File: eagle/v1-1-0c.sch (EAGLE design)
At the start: 177 parts, among them J1 CR22A-44D-2.54DSA(70), J3 26-60-4040, J4 AUDIO_JACK_3.5MM_PTH, J5 DIN5, SW1 3PDT-AQ-SWITCH, SW2 9077-1, U10 7805, U11 74LS10N, U13 74LS04N, U14 4528N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

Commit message: Errata updates to BRD and SCH and PDFs
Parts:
- added JP5, JP6: (no value), aquarius2:PINHD-1X1
- R49: device aq-rcl:R-US_0207/7 -> aq-rcl:R-US_0207/10
- R50, R51: value ∞/56k -> ∞/1.5k
- R52: value ∞/56k -> ∞/100
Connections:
- new net 2Φ-NTSC: JP5.1, U11A.O
- net 2Φ: now also JP6.1; no longer U11A.O
- net GND: no longer R49.1
- net VCC: now also R49.1
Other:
- note added: "(NTSC to GND)"
- note added: "(PAL through R49)"
- note added: "18 OCT 2020"
- note added: "NTSC Close for 2Φ"
- note removed: "(NTSC passthrough)"
- note removed: "05 SEP 2020"
- moved on the sheet: R49
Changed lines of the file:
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@@
 <part name="C2" library="aq-rcl" deviceset="C-US" device="050-024X044" package3d_urn="urn:adsk.eagle:package:23643/1" value="10pF"/>
 <part name="C25" library="aq-rcl" deviceset="C-US" device="050-025X090" value=".1uF"/>
-<part name="R49" library="aq-rcl" deviceset="R-US_" device="0207/7" package3d_urn="urn:adsk.eagle:package:23493/2" value="0/220"/>
 <part name="C37" library="aq-rcl" deviceset="C-US" device="025-030X050" package3d_urn="urn:adsk.eagle:package:23631/1" value=".001uF/∞"/>
 <part name="C1" library="aq-rcl" deviceset="CPOL-US" device="E2.5-6" package3d_urn="urn:adsk.eagle:package:23349/1" value="1uF @ 50v"/>
@@
 <part name="GND37" library="supply1" library_urn="urn:adsk.eagle:library:371" deviceset="GND" device=""/>
 <part name="P+11" library="supply1" library_urn="urn:adsk.eagle:library:371" deviceset="VCC" device=""/>
-<part name="GND13" library="supply1" library_urn="urn:adsk.eagle:library:371" deviceset="GND" device=""/>
 <part name="SUPPLY13" library="supply2" library_urn="urn:adsk.eagle:library:372" deviceset="VPP" device=""/>
 <part name="C23" library="aq-rcl" deviceset="C-US" device="050-024X044" package3d_urn="urn:adsk.eagle:package:23643/1" value="∞/10pF"/>
-<part name="R50" library="aq-rcl" deviceset="R-US_" device="0207/10" package3d_urn="urn:adsk.eagle:package:23491/2" value="∞/56k"/>
-<part name="R51" library="aq-rcl" deviceset="R-US_" device="0207/10" package3d_urn="urn:adsk.eagle:package:23491/2" value="∞/56k"/>
+<part name="R50" library="aq-rcl" deviceset="R-US_" device="0207/10" package3d_urn="urn:adsk.eagle:package:23491/2" value="∞/1.5k"/>
+<part name="R51" library="aq-rcl" deviceset="R-US_" device="0207/10" package3d_urn="urn:adsk.eagle:package:23491/2" value="∞/1.5k"/>
 <part name="XTAL2" library="special" library_urn="urn:adsk.eagle:library:367" deviceset="XTAL" device="" package3d_urn="urn:adsk.eagle:package:26649/1" value="∞/7.15909 Mhz"/>
-<part name="R52" library="aq-rcl" deviceset="R-US_" device="0207/10" package3d_urn="urn:adsk.eagle:package:23491/2" value="∞/56k"/>
+<part name="R52" library="aq-rcl" deviceset="R-US_" device="0207/10" package3d_urn="urn:adsk.eagle:package:23491/2" value="∞/100"/>
 <part name="U13" library="74xx-us" library_urn="urn:adsk.eagle:library:88" deviceset="74*04" device="N" package3d_urn="urn:adsk.eagle:package:16407/2" technology="LS"/>
 <part name="C43" library="aq-rcl" deviceset="C-US" device="050-025X090" value="∞/0.1uF"/>
@@
 <part name="SUPPLY12" library="supply2" library_urn="urn:adsk.eagle:library:372" deviceset="VEE" device=""/>
 <part name="J2" library="aquarius2" deviceset="PINHD-1X17" device="" package3d_urn="urn:adsk.eagle:package:22490/2"/>
+<part name="R49" library="aq-rcl" deviceset="R-US_" device="0207/10" package3d_urn="urn:adsk.eagle:package:23491/2" value="0/220"/>
+<part name="P+21" library="supply1" library_urn="urn:adsk.eagle:library:371" deviceset="VCC" device=""/>
+<part name="GND13" library="supply1" library_urn="urn:adsk.eagle:library:371" deviceset="GND" device=""/>
+<part name="JP5" library="aquarius2" deviceset="PINHD-1X1" device="" package3d_urn="urn:adsk.eagle:package:22485/2"/>
+<part name="JP6" library="aquarius2" deviceset="PINHD-1X1" device="" package3d_urn="urn:adsk.eagle:package:22485/2"/>
 </parts>
 <sheets>
@@
 <wire x1="261.62" y1="15.24" x2="261.62" y2="5.08" width="0.1524" layer="97"/>
 <wire x1="261.62" y1="5.08" x2="347.98" y2="5.08" width="0.1524" layer="97"/>
-<text x="304.8" y="7.62" size="5.08" layer="97" align="bottom-center">05 SEP 2020</text>
+<text x="304.8" y="7.62" size="5.08" layer="97" align="bottom-center">18 OCT 2020</text>
 <wire x1="347.98" y1="15.24" x2="347.98" y2="25.4" width="0.1524" layer="97"/>
 <wire x1="347.98" y1="25.4" x2="261.62" y2="25.4" width="0.1524" layer="97"/>
@@
 <wire x1="76.708" y1="59.436" x2="60.198" y2="59.436" width="0.1524" layer="97" style="shortdash"/>
 <wire x1="59.436" y1="59.436" x2="59.436" y2="67.818" width="0.1524" layer="97" style="shortdash"/>
-<text x="338.836" y="188.214" size="1.778" layer="97" distance="25" align="center">(NTSC passthrough)</text>
-<text x="343.916" y="194.056" size="1.016" layer="97" distance="25" rot="R180" align="center">NTSC to JP4
+<text x="343.154" y="187.96" size="1.27" layer="97" distance="25" align="center">(NTSC to GND)</text>
+<text x="344.424" y="195.072" size="1.016" layer="97" distance="25" rot="R180" align="center">NTSC to JP4
 TEA1002 PALSW</text>
 <text x="268.732" y="258.064" size="1.016" layer="97" distance="25" rot="R180" align="center">PAL to JP4
@@
 <text x="30.48" y="86.36" size="2.54" layer="97" align="center">AUX Power
 Header</text>
+<wire x1="350.52" y1="190.5" x2="350.52" y2="185.42" width="0.1524" layer="97" style="shortdash"/>
+<text x="330.454" y="192.024" size="1.27" layer="97" distance="25" align="center">(PAL through R49)</text>
+<text x="401.32" y="165.1" size="1.016" layer="97" distance="25" rot="R180" align="center">NTSC Close
+for 2Φ</text>
 </plain>
 <instances>
@@
 <attribute name="VALUE" x="378.968" y="174.625" size="1.778" layer="96" rot="MR180"/>
 </instance>
-<instance part="R49" gate="G$1" x="325.12" y="190.5" smashed="yes">
-<attribute name="NAME" x="321.31" y="191.9986" size="1.778" layer="95"/>
-<attribute name="VALUE" x="321.31" y="187.198" size="1.778" layer="96"/>
-</instance>
 <instance part="C37" gate="G$1" x="538.48" y="190.5" smashed="yes" rot="R90">
 <attribute name="NAME" x="535.432" y="196.215" size="1.778" layer="95"/>
@@
 <attribute name="VALUE" x="612.14" y="307.34" size="1.778" layer="96" rot="R90"/>
 </instance>
-<instance part="GND13" gate="1" x="307.34" y="190.5" smashed="yes" rot="R270">
-<attribute name="VALUE" x="304.8" y="193.04" size="1.778" layer="96" rot="R270"/>
-</instance>
 <instance part="SUPPLY13" gate="G$1" x="497.84" y="134.62" smashed="yes" rot="R270">
 <attribute name="VALUE" x="501.015" y="136.525" size="1.778" layer="96" rot="R270"/>
@@
 <attribute name="VALUE" x="106.68" y="156.21" size="1.778" layer="96" rot="MR270"/>
 </instance>
+<instance part="R49" gate="G$1" x="317.5" y="190.5" smashed="yes">
+<attribute name="NAME" x="313.69" y="191.9986" size="1.778" layer="95"/>
+<attribute name="VALUE" x="313.69" y="187.198" size="1.778" layer="96"/>
+</instance>
+<instance part="P+21" gate="VCC" x="307.34" y="190.5" smashed="yes" rot="R90">
+<attribute name="VALUE" x="306.578" y="190.5" size="1.778" layer="96" rot="R180"/>
+</instance>
+<instance part="GND13" gate="1" x="350.52" y="182.88" smashed="yes" rot="MR0">
+<attribute name="VALUE" x="353.06" y="180.34" size="1.778" layer="96" rot="MR0"/>
+</instance>
+<instance part="JP5" gate="G$1" x="398.78" y="154.94" smashed="yes" rot="R270">
+<attribute name="VALUE" x="393.7" y="161.29" size="1.778" layer="96" rot="R270"/>
+</instance>
+<instance part="JP6" gate="G$1" x="403.86" y="154.94" smashed="yes" rot="R270">
+<attribute name="VALUE" x="398.78" y="161.29" size="1.778" layer="96" rot="R270"/>
+</instance>
 </instances>
 <busses>
@@
 </segment>
 <segment>
-<wire x1="320.04" y1="190.5" x2="309.88" y2="190.5" width="0.1524" layer="91"/>
-<pinref part="R49" gate="G$1" pin="1"/>
-<pinref part="GND13" gate="1" pin="GND"/>
-</segment>
-<segment>
 <pinref part="C26" gate="G$1" pin="2"/>
 <wire x1="127" y1="309.88" x2="124.46" y2="309.88" width="0.1524" layer="91"/>
@@
 <wire x1="25.4" y1="71.12" x2="25.4" y2="73.66" width="0.1524" layer="91"/>
 </segment>
+<segment>
+<pinref part="R49" gate="G$1" pin="1"/>
+<wire x1="312.42" y1="190.5" x2="309.88" y2="190.5" width="0.1524" layer="91"/>
+<pinref part="P+21" gate="VCC" pin="VCC"/>
+</segment>
 </net>
 <net name="N$767" class="0">
@@
 <net name="2Φ" class="0">
 <segment>
-<pinref part="U11" gate="A" pin="O"/>
-<wire x1="393.7" y1="162.56" x2="401.32" y2="162.56" width="0.1524" layer="91"/>
-<label x="401.32" y="162.56" size="1.27" layer="95" xref="yes"/>
-</segment>
-<segment>
 <pinref part="U6" gate="A" pin="CLK"/>
 <wire x1="200.66" y1="203.2" x2="203.2" y2="203.2" width="0.1524" layer="91"/>
@@
 <label x="668.02" y="55.88" size="1.016" layer="95" xref="yes"/>
 </segment>
+<segment>
+<pinref part="JP6" gate="G$1" pin="1"/>
+<wire x1="403.86" y1="157.48" x2="403.86" y2="162.56" width="0.1524" layer="91"/>
+<wire x1="403.86" y1="162.56" x2="406.4" y2="162.56" width="0.1524" layer="91"/>
+<label x="406.4" y="162.56" size="1.016" layer="95" xref="yes"/>
+</segment>
 </net>
 <net name="XA14" class="0">
@@
 <segment>
 <pinref part="U7" gate="G$1" pin="!525!/625"/>
-<pinref part="R49" gate="G$1" pin="2"/>
 <wire x1="350.52" y1="220.98" x2="350.52" y2="190.5" width="0.1524" layer="91"/>
-<wire x1="330.2" y1="190.5" x2="342.9" y2="190.5" width="0.1524" layer="91"/>
+<wire x1="322.58" y1="190.5" x2="342.9" y2="190.5" width="0.1524" layer="91"/>
 <wire x1="342.9" y1="190.5" x2="350.52" y2="190.5" width="0.1524" layer="91"/>
 <wire x1="340.36" y1="220.98" x2="350.52" y2="220.98" width="0.1524" layer="91"/>
+<pinref part="R49" gate="G$1" pin="2"/>
 </segment>
 </net>
@@
 </segment>
 </net>
+<net name="2Φ-NTSC" class="0">
+<segment>
+<pinref part="U11" gate="A" pin="O"/>
+<pinref part="JP5" gate="G$1" pin="1"/>
+<wire x1="393.7" y1="162.56" x2="398.78" y2="162.56" width="0.1524" layer="91"/>
+<wire x1="398.78" y1="162.56" x2="398.78" y2="157.48" width="0.1524" layer="91"/>
+</segment>
+</net>

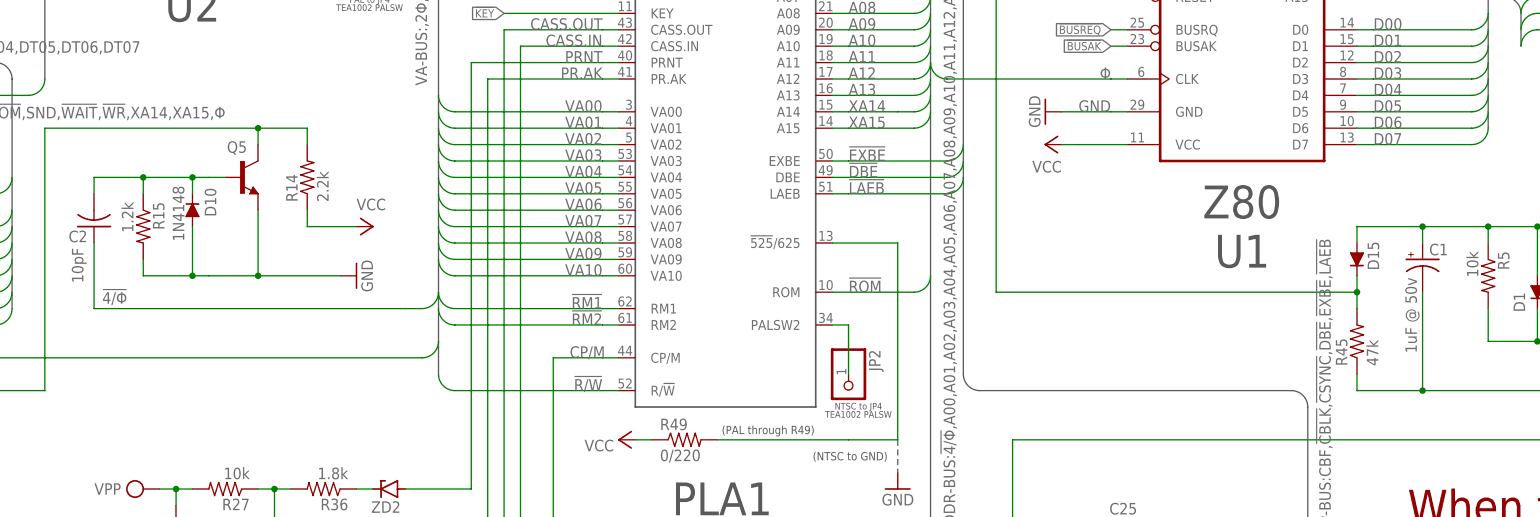
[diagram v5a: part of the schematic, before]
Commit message: 19 OCT 2020 fixes from Errata
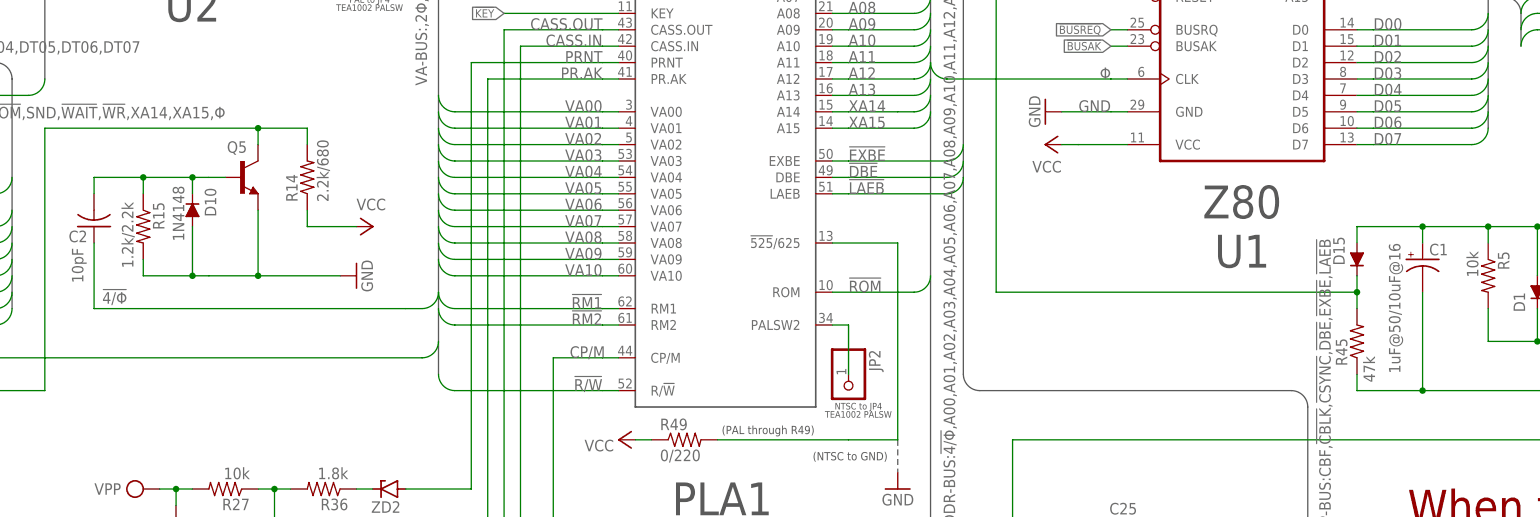
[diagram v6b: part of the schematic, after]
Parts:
- C1: value 1uF @ 50v -> 1uF@50/10uF@16
- R14: value 2.2k -> 2.2k/680
- R15: value 1.2k -> 1.2k/2.2k
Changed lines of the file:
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@@
 <part name="R8" library="aq-rcl" deviceset="R-US_" device="0207/10" package3d_urn="urn:adsk.eagle:package:23491/2" value="820"/>
 <part name="R9" library="aq-rcl" deviceset="R-US_" device="0207/10" package3d_urn="urn:adsk.eagle:package:23491/2" value="820"/>
-<part name="R14" library="aq-rcl" deviceset="R-US_" device="0207/10" package3d_urn="urn:adsk.eagle:package:23491/2" value="2.2k"/>
-<part name="R15" library="aq-rcl" deviceset="R-US_" device="0207/10" package3d_urn="urn:adsk.eagle:package:23491/2" value="1.2k"/>
+<part name="R14" library="aq-rcl" deviceset="R-US_" device="0207/10" package3d_urn="urn:adsk.eagle:package:23491/2" value="2.2k/680"/>
+<part name="R15" library="aq-rcl" deviceset="R-US_" device="0207/10" package3d_urn="urn:adsk.eagle:package:23491/2" value="1.2k/2.2k"/>
 <part name="R55" library="aq-rcl" deviceset="R-US_" device="0207/10" package3d_urn="urn:adsk.eagle:package:23491/2" value="47k/∞"/>
 <part name="R5" library="aq-rcl" deviceset="R-US_" device="0207/10" package3d_urn="urn:adsk.eagle:package:23491/2" value="10k"/>
@@
 <part name="C25" library="aq-rcl" deviceset="C-US" device="050-025X090" value=".1uF"/>
 <part name="C37" library="aq-rcl" deviceset="C-US" device="025-030X050" package3d_urn="urn:adsk.eagle:package:23631/1" value=".001uF/∞"/>
-<part name="C1" library="aq-rcl" deviceset="CPOL-US" device="E2.5-6" package3d_urn="urn:adsk.eagle:package:23349/1" value="1uF @ 50v"/>
+<part name="C1" library="aq-rcl" deviceset="CPOL-US" device="E2.5-6" package3d_urn="urn:adsk.eagle:package:23349/1" value="1uF@50/10uF@16"/>
 <part name="C22" library="aq-rcl" deviceset="C-US" device="050-025X085" value=".1uF"/>
 <part name="C26" library="aq-rcl" deviceset="C-US" device="050-025X085" value=".1uF"/>
@@
 <instance part="R45" gate="G$1" x="421.64" y="205.74" smashed="yes" rot="R90">
 <attribute name="NAME" x="420.1414" y="201.93" size="1.778" layer="95" rot="R90"/>
-<attribute name="VALUE" x="424.942" y="201.93" size="1.778" layer="96" rot="R90"/>
+<attribute name="VALUE" x="424.434" y="199.39" size="1.778" layer="96" rot="R90"/>
 </instance>
 <instance part="R24" gate="G$1" x="289.56" y="73.66" smashed="yes" rot="R270">
@@
 </instance>
 <instance part="D15" gate="G$1" x="421.64" y="218.44" smashed="yes" rot="MR270">
-<attribute name="NAME" x="425.069" y="221.234" size="1.778" layer="95" rot="MR270"/>
+<attribute name="NAME" x="419.735" y="221.996" size="1.778" layer="95" rot="MR270"/>
 </instance>
 <instance part="D12" gate="G$1" x="342.9" y="58.42" smashed="yes" rot="MR90">
@@
 <instance part="C1" gate="G$1" x="431.8" y="218.44" smashed="yes">
 <attribute name="NAME" x="432.816" y="219.075" size="1.778" layer="95"/>
-<attribute name="VALUE" x="429.133" y="215.646" size="1.778" layer="96" rot="R270"/>
+<attribute name="VALUE" x="426.593" y="220.98" size="1.778" layer="96" rot="R270"/>
 </instance>
 <instance part="C22" gate="G$1" x="53.34" y="309.88" smashed="yes" rot="MR90">
